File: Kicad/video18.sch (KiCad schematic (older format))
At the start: 18 parts, among them J201 DE15HD, U201 THS7316, U202 TPD7S019

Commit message: Brought in sheets from Neotron Pico.
Also includes DB15HD and PSU 3D models.
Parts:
- J201: footprint Connector_Dsub:DSUB-15-HD_Female_Horizontal_P2.29x1.98mm_EdgePinOffset3.03mm_Housed_MountingHolesOffset4.94mm -> Neotron-Common-Hardware:Amphenol_ICD15S13E4GV00LF
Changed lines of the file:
@@
 $Descr A4 11693 8268
 encoding utf-8
-Sheet 2 17
-Title "Neotron Common Hardware - Video Output"
-Date "2021-04-02"
+Sheet 2 18
+Title "Neotron Common Hardware"
+Date "2021-06-18"
 Rev "[Uncontrolled]"
 Comp "https://neotron-compute.github.io/"
@@
 F 0 "J201" H 9250 4850 50  0000 L CNN
 F 1 "DE15HD" H 9350 4800 50  0000 C TNN
-F 2 "Connector_Dsub:DSUB-15-HD_Female_Horizontal_P2.29x1.98mm_EdgePinOffset3.03mm_Housed_MountingHolesOffset4.94mm" H 8400 4400 50  0001 C CNN
+F 2 "Neotron-Common-Hardware:Amphenol_ICD15S13E4GV00LF" H 8400 4400 50  0001 C CNN
 F 3 "~" H 8400 4400 50  0001 C CNN
 F 4 "0" H 9350 4000 50  0001 C CNN "DNP"

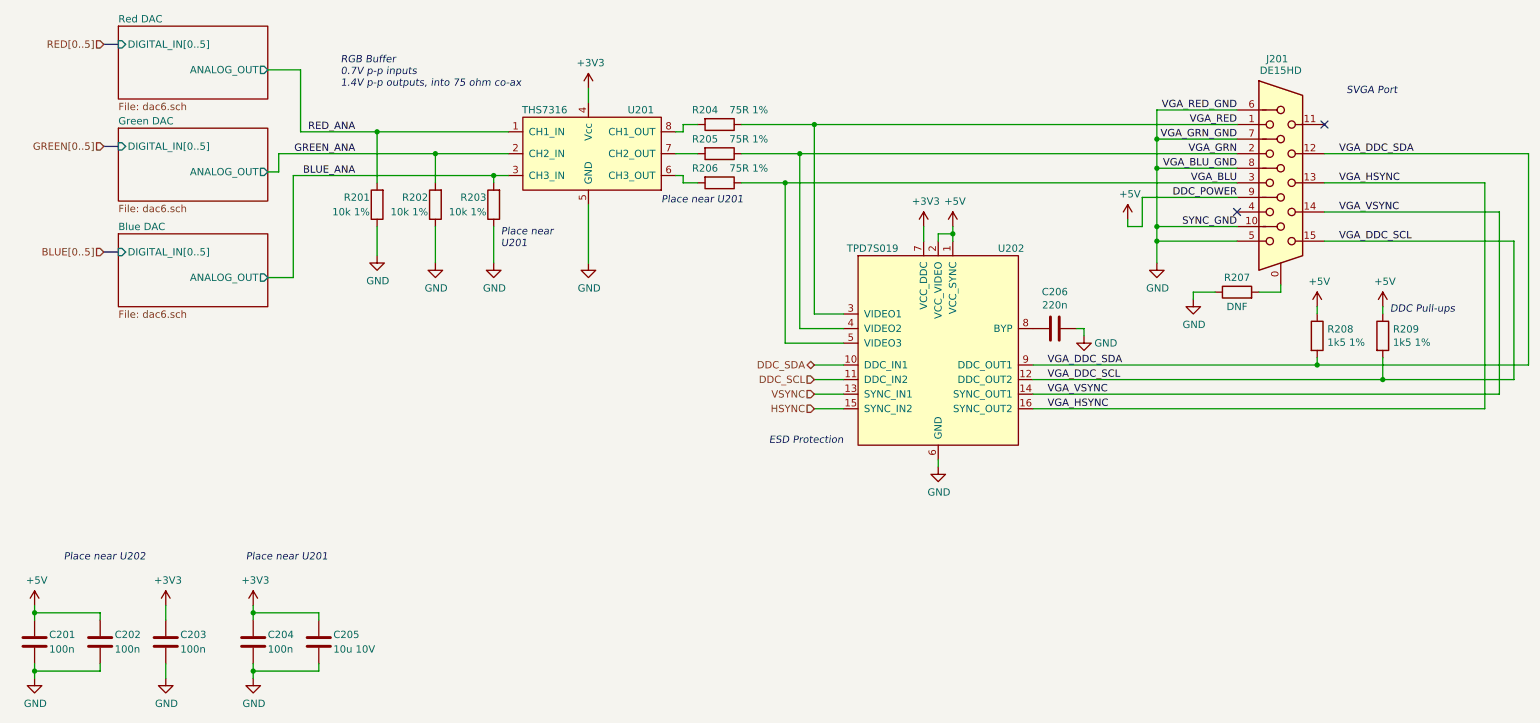
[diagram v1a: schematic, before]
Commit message: Merge in more changes.
Mostly lowering voltage tolerances to minimum required.
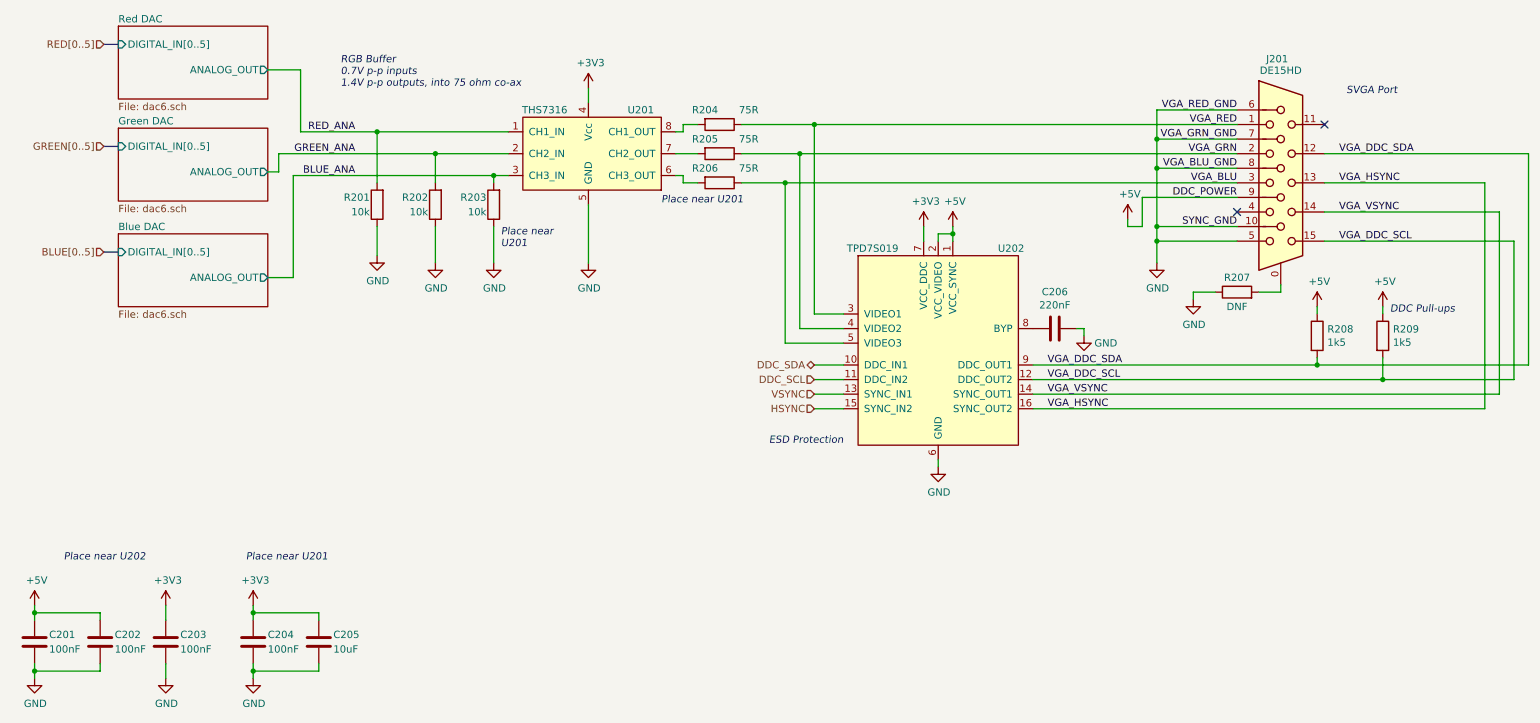
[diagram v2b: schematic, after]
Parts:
- C201, C202: value 100n -> 100nF; MPN K104K15X7RF5TL2 -> CPL-CAP-X7R-0805-100NF-50V; Tolerance (none) -> X5R; Voltage (none) -> 16V
- C203, C204: value 100n -> 100nF; MPN K104K15X7RF5TL2 -> CPL-CAP-X7R-0805-100NF-50V; Tolerance (none) -> X5R; Voltage (none) -> 10V
- C205: value 10u 10V -> 10uF; MPN CL21A106KOQNNNG -> CPL-CAP-X5R-0805-10UF-16V; Tolerance (none) -> X5R; Voltage (none) -> 10V
- C206: value 220n -> 220nF; Tolerance (none) -> X5R; Voltage (none) -> 50V
- R201, R202, R203: value 10k 1% -> 10k; MPN RMCF0805FT10K0 -> CPL-RES-0805-10K-0.125W; Tolerance (none) -> 1%
- R204, R205, R206: value 75R 1% -> 75R; Tolerance (none) -> 1%
- R208, R209: value 1k5 1% -> 1k5; Tolerance (none) -> 1%
- U201: MPN THS7316 -> THS7316DR
- U202: MPN TPD7S019 -> TPD7S019-15DBQR
